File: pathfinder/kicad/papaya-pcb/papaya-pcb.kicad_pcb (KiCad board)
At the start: 2 copper layers, 70 x 90 mm, 12 parts, among them J1 J1 (2 pins), J10 J_S2 (3 pins), J11 J_S3 (3 pins), J12 J_S4 (3 pins), J2 J_ESP32 (13 pins), J3 J_UBEC5V (4 pins), J4 J_BTS1 (6 pins), J5 J_BTS2 (6 pins), J6 J_ELRS (4 pins), J7 J_GND_MASTER (1 pins), J8 J_UBEC6V (2 pins), J9 J_S1 (3 pins)

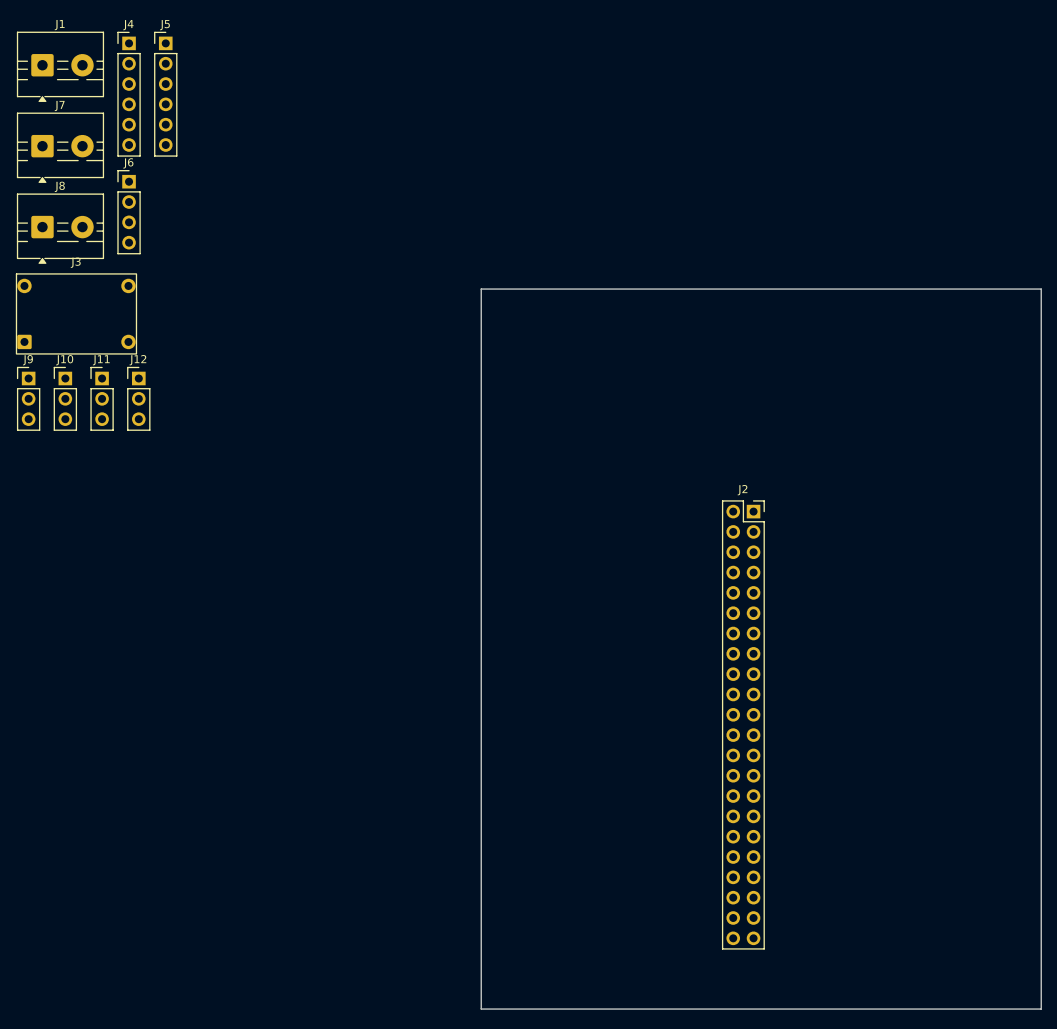
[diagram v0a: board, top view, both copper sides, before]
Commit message: Commit with components on the board pending trace layouts.
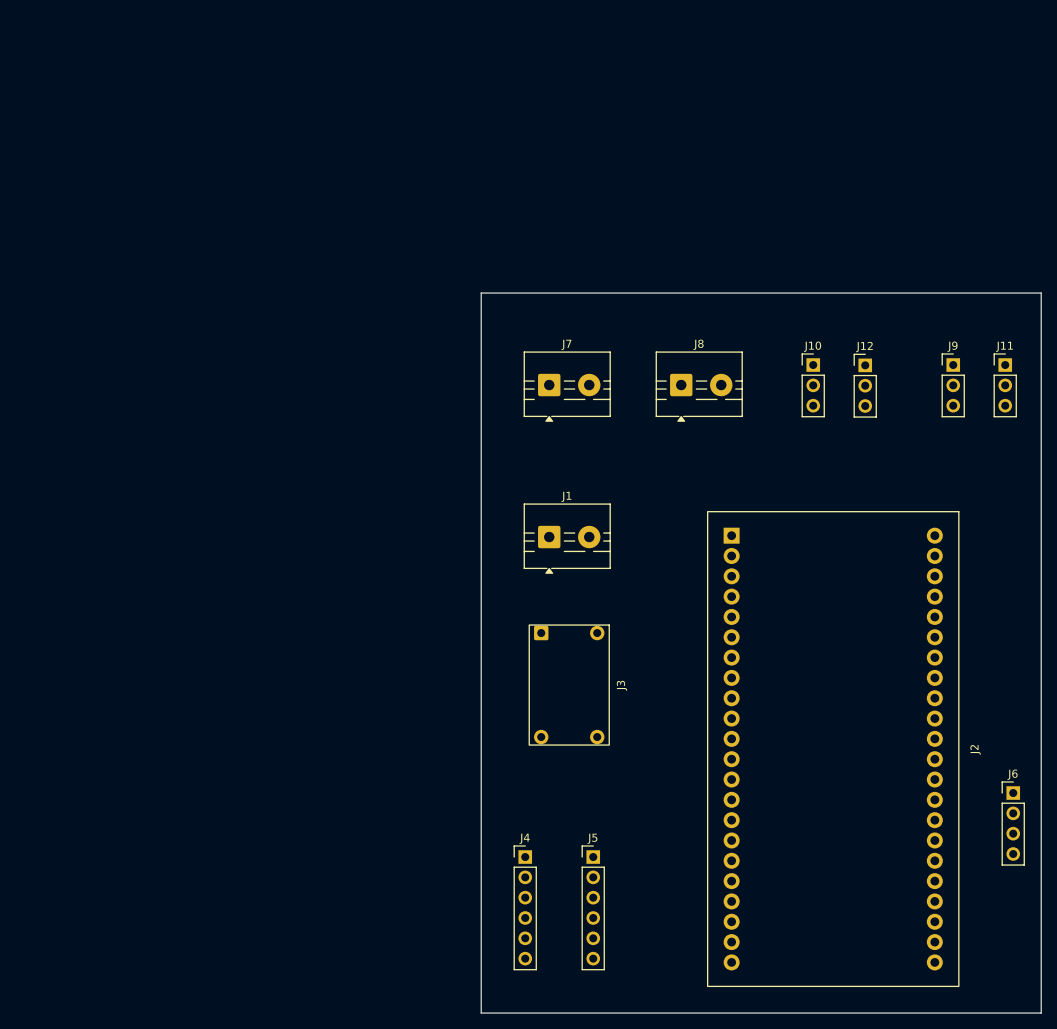
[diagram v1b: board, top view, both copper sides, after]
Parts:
- J10, J11, J12, J9: footprint Connector_PinHeader_2.54mm:PinHeader_1x03_P2.54mm_Vertical -> papaya-pcb:PinHeader_1x03_Servo
- J2: footprint Connector_PinSocket_2.54mm:PinSocket_2x22_P2.54mm_Vertical -> papaya-pcb:ESP32S3_DevKit_2x1x22_split
- J4, J5: footprint Connector_PinHeader_2.54mm:PinHeader_1x06_P2.54mm_Vertical -> papaya-pcb:PinHeader_1x06_BTS_Signal
- J6: footprint Connector_PinHeader_2.54mm:PinHeader_1x04_P2.54mm_Vertical -> papaya-pcb:PinHeader_1x04_ELRS
- J8: footprint TerminalBlock:TerminalBlock_MaiXu_MX126-5.0-02P_1x02_P5.00mm -> papaya-pcb:TerminalBlock_2Pos_UBEC6V
- moved J6 134.4 mm to (157.0, 121.0)
- moved J9 115.6 mm to (149.5, 67.5)
- moved J5 114.9 mm to (104.5, 129.0)
- moved J4 113.1 mm to (96.0, 129.0)
- moved J11 112.9 mm to (156.0, 67.5)
- moved J10 93.5 mm to (132.0, 67.5)
- moved J12 90.8 mm to (138.5, 67.5)
- moved J1 86.5 mm to (99.0, 89.0)
- moved J8 82.3 mm to (115.5, 70.0)
- moved J3 77.1 mm to (101.5, 107.5), turned to -90 degrees
- moved J7 70.0 mm to (99.0, 70.0)
- moved J2 31.3 mm to (134.5, 115.5), turned to -90 degrees
